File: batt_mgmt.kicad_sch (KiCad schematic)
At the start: 57 parts, among them Q1 DMN2014LHAB-7, Q2 DMP3056L, U1 BQ24074RGT, U2 BQ29728, U3 BQ27427

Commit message: Configured Varients
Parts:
- added R17: 0R, Resistor_SMD:R_1206_3216Metric, symbol Device:R_US
- renumbered R17 to R18, R18 to R19, R19 to R20
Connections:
- net +CELL: now also R17.1
- net +PACK: now also R17.2
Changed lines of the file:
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@@
 	)
 	(junction
+		(at 245.11 39.37)
+		(diameter 0)
+		(color 0 0 0 0)
+	)
+	(junction
 		(at 233.68 134.62)
 		(diameter 0)
@@
 	)
 	(junction
+		(at 234.95 39.37)
+		(diameter 0)
+		(color 0 0 0 0)
+	)
+	(junction
 		(at 177.8 149.86)
 		(diameter 0)
@@
 	(wire
 		(pts
+			(xy 243.84 30.48) (xy 245.11 30.48)
+		)
+		(stroke
+			(width 0)
+			(type default)
+		)
+	)
+	(wire
+		(pts
 			(xy 105.41 54.61) (xy 149.86 54.61)
 		)
@@
 	(wire
 		(pts
+			(xy 236.22 30.48) (xy 234.95 30.48)
+		)
+		(stroke
+			(width 0)
+			(type default)
+		)
+	)
+	(wire
+		(pts
 			(xy 162.56 132.08) (xy 167.64 132.08)
 		)
@@
 	(wire
 		(pts
+			(xy 234.95 30.48) (xy 234.95 39.37)
+		)
+		(stroke
+			(width 0)
+			(type default)
+		)
+	)
+	(wire
+		(pts
 			(xy 113.03 138.43) (xy 119.38 138.43)
 		)
@@
 	(wire
 		(pts
+			(xy 245.11 30.48) (xy 245.11 39.37)
+		)
+		(stroke
+			(width 0)
+			(type default)
+		)
+	)
+	(wire
+		(pts
 			(xy 223.52 109.22) (xy 224.79 109.22)
 		)
@@
 	)
 	(symbol
+		(lib_id "Device:R_US")
+		(at 240.03 30.48 90)
+		(unit 1)
+		(body_style 1)
+		(exclude_from_sim no)
+		(in_bom yes)
+		(on_board yes)
+		(in_pos_files yes)
+		(dnp yes)
+		(property "Reference" "R17"
+			(at 237.744 27.94 90)
+			(show_name no)
+			(do_not_autoplace no)
+			(effects
+				(font
+					(size 1.27 1.27)
+				)
+				(justify left)
+			)
+		)
+		(property "Value" "0R"
+			(at 240.538 27.94 90)
+			(show_name no)
+			(do_not_autoplace no)
+			(effects
+				(font
+					(size 1.27 1.27)
+				)
+				(justify left)
+			)
+		)
+		(property "Footprint" "Resistor_SMD:R_1206_3216Metric"
+			(at 240.284 29.464 90)
+			(hide yes)
+			(show_name no)
+			(do_not_autoplace no)
+			(effects
+				(font
+					(size 1.27 1.27)
+				)
+			)
+		)
+		(property "Datasheet" ""
+			(at 240.03 30.48 0)
+			(hide yes)
+			(show_name no)
+			(do_not_autoplace no)
+			(effects
+				(font
+					(size 1.27 1.27)
+				)
+			)
+		)
+		(property "Description" "Resistor, US symbol"
+			(at 240.03 30.48 0)
+			(hide yes)
+			(show_name no)
+			(do_not_autoplace no)
+			(effects
+				(font
+					(size 1.27 1.27)
+				)
+			)
+		)
+		(property "MFR#" "HP06W2J0000T5E"
+			(at 240.03 30.48 0)
+			(hide yes)
+			(show_name no)
+			(do_not_autoplace no)
+			(effects
+				(font
+					(size 1.27 1.27)
+				)
+			)
+		)
+		(property "Package" "1206"
+			(at 240.03 30.48 0)
+			(hide yes)
+			(show_name no)
+			(do_not_autoplace no)
+			(effects
+				(font
+					(size 1.27 1.27)
+				)
+			)
+		)
+		(property "LCSC#" "C473612"
+			(at 240.03 30.48 0)
+			(hide yes)
+			(show_name no)
+			(do_not_autoplace no)
+			(effects
+				(font
+					(size 1.27 1.27)
+				)
+			)
+		)
+		(pin "2"
+		)
+		(pin "1"
+		)
+		(instances
+			(project "power_module"
+				(path "/33e2b92e-f705-4be7-96f4-57092b8ec1ea/d3495413-1b7d-4fcf-bddf-7a80ce18b16c"
+					(reference "R17")
+					(unit 1)
+					(variant
+						(name "5v Dumb")
+					)
+				)
+			)
+		)
+	)
+	(symbol
 		(lib_id "power:+5V")
 		(at 81.28 138.43 0)
@@
 					(reference "R12")
 					(unit 1)
+					(variant
+						(name "3v3 Dumb")
+						(dnp yes)
+					)
+					(variant
+						(name "5v Dumb")
+						(dnp yes)
+					)
 				)
 			)
@@
 					(reference "R3")
 					(unit 1)
+					(variant
+						(name "3v3 Dumb")
+						(dnp no)
+					)
+					(variant
+						(name "5v Dumb")
+						(dnp no)
+					)
 				)
 			)
@@
 					(reference "R7")
 					(unit 1)
+					(variant
+						(name "3v3 Dumb")
+						(dnp no)
+					)
+					(variant
+						(name "5v Dumb")
+						(dnp no)
+					)
 				)
 			)
@@
 		(in_pos_files yes)
 		(dnp no)
-		(property "Reference" "R18"
+		(property "Reference" "R19"
 			(at 245.11 137.414 0)
 			(show_name no)
@@
 			(project "power_module"
 				(path "/33e2b92e-f705-4be7-96f4-57092b8ec1ea/d3495413-1b7d-4fcf-bddf-7a80ce18b16c"
-					(reference "R18")
+					(reference "R19")
 					(unit 1)
 				)
@@
 					(reference "R1")
 					(unit 1)
+					(variant
+						(name "3v3 Dumb")
+						(dnp no)
+					)
+					(variant
+						(name "5v Dumb")
+						(dnp no)
+					)
 				)
 			)
@@
 		(in_pos_files yes)
 		(dnp yes)
-		(property "Reference" "R19"
+		(property "Reference" "R20"
 			(at 249.936 88.646 0)
 			(show_name no)
@@
 			(project "power_module"
 				(path "/33e2b92e-f705-4be7-96f4-57092b8ec1ea/d3495413-1b7d-4fcf-bddf-7a80ce18b16c"
-					(reference "R19")
+					(reference "R20")
 					(unit 1)
+					(variant
+						(name "3v3 Dumb")
+						(dnp no)
+					)
+					(variant
+						(name "5v Dumb")
+						(dnp no)
+					)
 				)
 			)
@@
 					(reference "R11")
 					(unit 1)
+					(variant
+						(name "3v3 Dumb")
+						(dnp no)
+					)
+					(variant
+						(name "5v Dumb")
+						(dnp no)
+					)
 				)
 			)
@@
 					(reference "U3")
 					(unit 1)
+					(variant
+						(name "3v3 Dumb")
+						(dnp yes)
+					)
+					(variant
+						(name "5v Dumb")
+						(dnp yes)
+					)
 				)
 			)
@@
 					(reference "R14")
 					(unit 1)
+					(variant
+						(name "3v3 Dumb")
+						(dnp yes)
+					)
+					(variant
+						(name "5v Dumb")
+						(dnp yes)
+					)
 				)
 			)
@@
 		(in_pos_files yes)
 		(dnp no)
-		(property "Reference" "R17"
+		(property "Reference" "R18"
 			(at 241.046 52.324 0)
 			(show_name no)
@@
 			(project "power_module"
 				(path "/33e2b92e-f705-4be7-96f4-57092b8ec1ea/d3495413-1b7d-4fcf-bddf-7a80ce18b16c"
-					(reference "R17")
+					(reference "R18")
 					(unit 1)
 				)
@@
 					(reference "C6")
 					(unit 1)
+					(variant
+						(name "3v3 Dumb")
+						(dnp yes)
+					)
+					(variant
+						(name "5v Dumb")
+						(dnp yes)
+					)
 				)
 			)
@@
 					(reference "C5")
 					(unit 1)
+					(variant
+						(name "3v3 Dumb")
+						(dnp yes)
+					)
+					(variant
+						(name "5v Dumb")
+						(dnp yes)
+					)
 				)
 			)

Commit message: Moved charger configuration resistors to own block
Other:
- note added: "BQ24074 Charge Controller Settings"
- note added: "Enable Pins BQ24074 Charge Controller"
- moved on the sheet: C1, C2, R1, R2, R3, R4, R5, R6, R7, R8, R9, TP1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

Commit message: Arranged functional blocks
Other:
- note added: "BQ24074 Charge Controller Enable Pins"
- note added: "Li Ion Cell /w Optional Polarity Protection Circuit"
- note removed: "EN pin settings"
- note removed: "Enable Pins BQ24074 Charge Controller"
- note removed: "Li Ion Cell"
- moved on the sheet: BT1, C1, C2, C3, C4, C5, C6, LED1, LED2, Q1, Q2, R1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

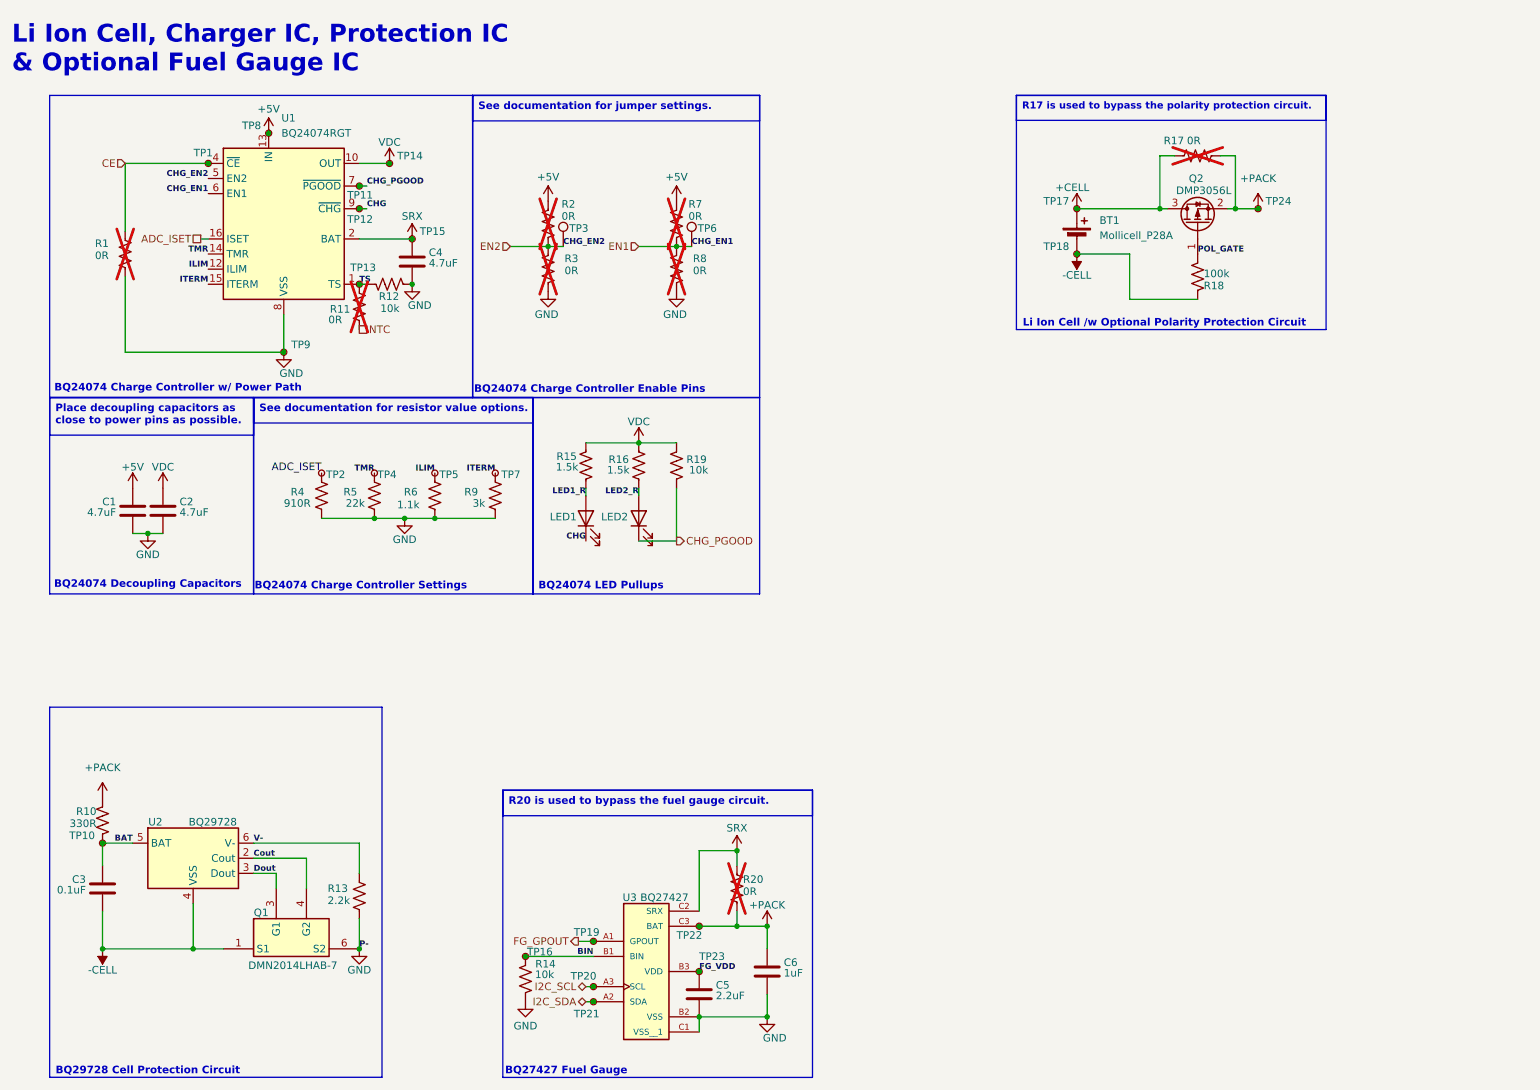
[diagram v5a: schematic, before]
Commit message: Started work on PCB layout
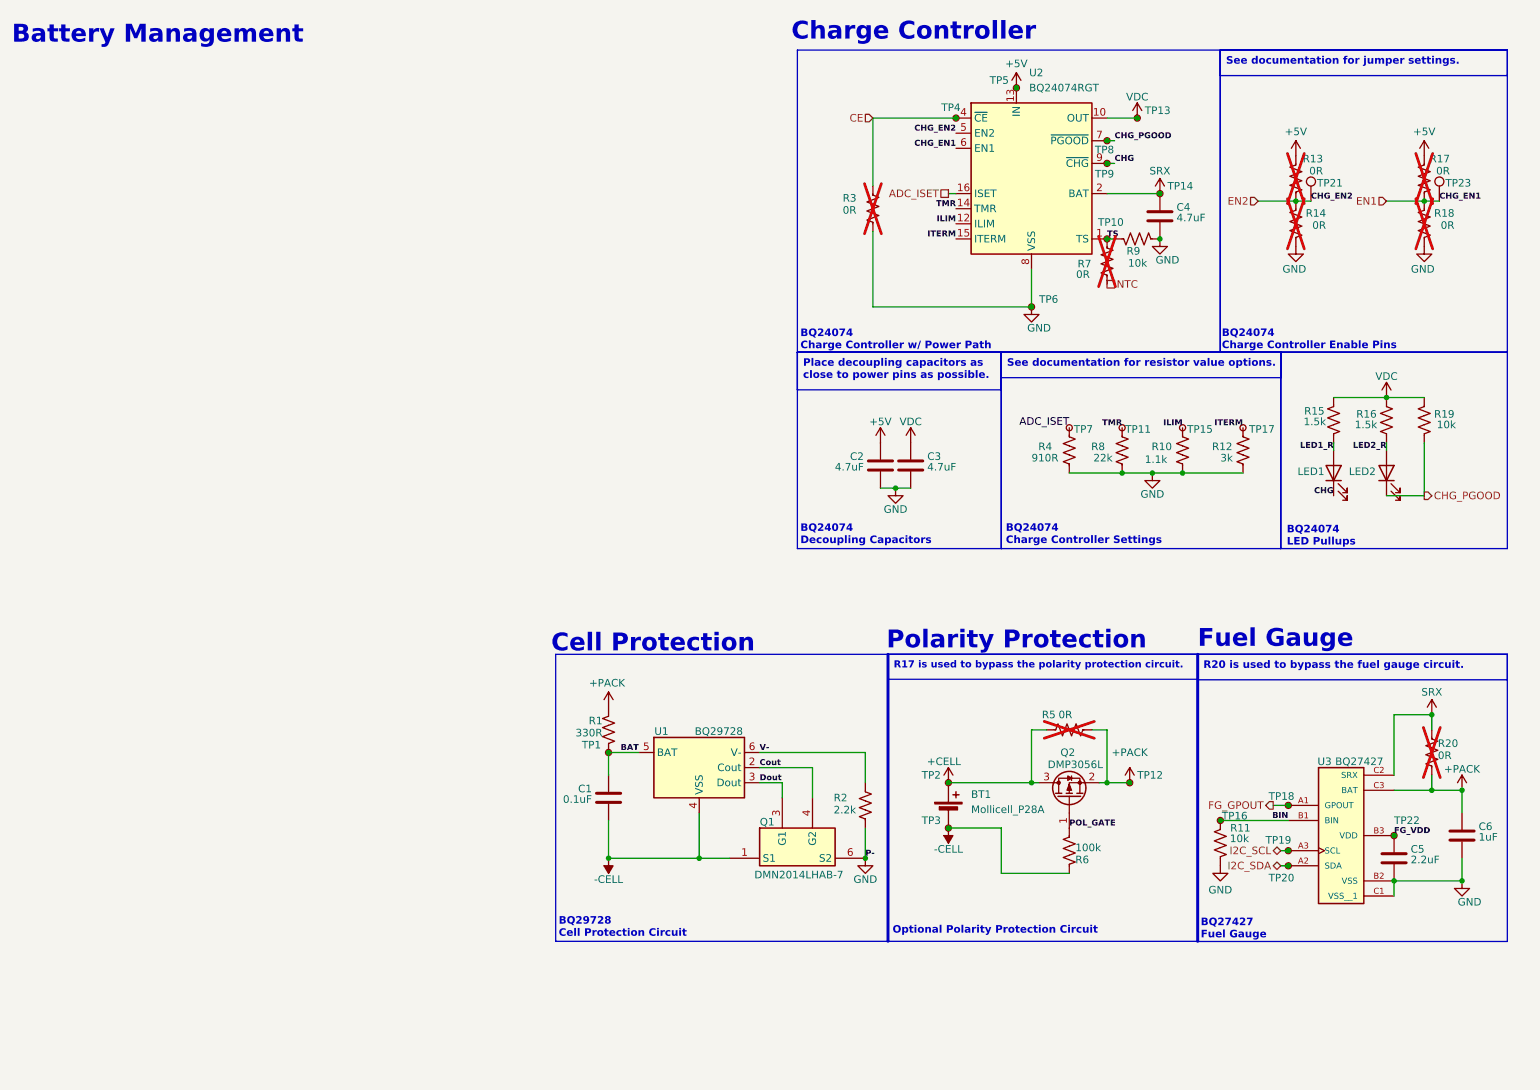
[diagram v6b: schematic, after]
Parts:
- removed TP22: FG_BATT, TestPoint:TestPoint_Pad_D1.0mm, symbol Connector:TestPoint_Small
- TP1: renamed from TP10; footprint (none) -> TestPoint:TestPoint_Pad_D1.0mm
- TP10: renamed from TP13; footprint (none) -> TestPoint:TestPoint_Pad_D1.0mm
- TP11: renamed from TP4; footprint (none) -> TestPoint:TestPoint_Pad_D1.0mm
- TP15: renamed from TP5; footprint (none) -> TestPoint:TestPoint_Pad_D1.0mm
- TP16: footprint (none) -> TestPoint:TestPoint_Pad_D1.0mm
- TP17: renamed from TP7; footprint (none) -> TestPoint:TestPoint_Pad_D1.0mm
- TP18: renamed from TP19; footprint (none) -> TestPoint:TestPoint_Pad_D1.0mm
- TP22: renamed from TP23; footprint (none) -> TestPoint:TestPoint_Pad_D1.0mm
- renumbered C3 to C1, C1 to C2, C2 to C3, R10 to R1, R6 to R10, R14 to R11, R9 to R12, R2 to R13, R3 to R14, R7 to R17, R8 to R18, R13 to R2, R1 to R3, R17 to R5, R18 to R6, R11 to R7, R5 to R8, R12 to R9, TP24 to TP12, TP14 to TP13, TP15 to TP14, TP20 to TP19, TP17 to TP2, TP21 to TP20, TP3 to TP21, TP6 to TP23, TP18 to TP3, TP1 to TP4, TP8 to TP5, TP9 to TP6, TP2 to TP7, TP11 to TP8, TP12 to TP9, U2 to U1, U1 to U2
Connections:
- net CHG: no longer U2.3 (BAT)
- net SRX: now also U2.3 (BAT)
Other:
- note added: "Battery Management"
- note added: "Cell Protection"
- note added: "Charge Controller"
- note added: "Fuel Gauge"
- note added: "Optional Polarity Protection Circuit"
- note added: "Polarity Protection"
- note removed: "Li Ion Cell /w Optional Polarity Protection Circuit"
- note removed: "Li Ion Cell, Charger IC, Protection IC & Optional Fuel Gauge IC"
- moved on the sheet: BT1, C1, C2, C3, C4, C5, C6, LED1, LED2, Q1, Q2, R1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

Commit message: Initial commit
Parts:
- removed Q2: DMP3056L, Package_TO_SOT_SMD:SOT-23, symbol Transistor_FET:Q_PMOS_GSD
- added Q2: DMP2008UFG-7, Package_SON:Diodes_PowerDI3333-8, symbol PowerMOSFET:DMP2008UFG-7
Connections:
- net +CELL: now also Q2.5 (D)
- net +PACK: now also Q2.1 (S), Q2.2 (S), Q2.3 (S)
- net POL_GATE: now also Q2.4 (G)
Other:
- moved on the sheet: R6, TP12
